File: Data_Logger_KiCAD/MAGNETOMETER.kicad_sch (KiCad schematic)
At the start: 0 parts

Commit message: Sub-schematics Generated
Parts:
- added C17: 10u, symbol Device:C
- added C18: 1u, symbol Device:C
- added U7: MMC5983MA, MMC5983MA_MEM, symbol MMC5983MA_FTP:MMC5983MA
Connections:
- new net: C17.1, U7.10 (CAP)
- new net +3.3V: C18.1, U7.13 (VDDIO), U7.2 (VDD)
- new net GND: C17.2, C18.2, U7.11 (GND), U7.9 (GND)
- new net INT: U7.15 (INT)
- new net SCL/SPI_SCK: U7.1 (SCL/SPI_SCK)
- new net SDA/SPI_SDI: U7.16 (SDA/SPI_SDI)
- new net SPI_CS: U7.4 (SPI_CS)
- new net SPI_SDO: U7.5 (SPI_SDO)
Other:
- company: (none) -> OSU ASDT
- title: (none) -> Magnetometer Schematic

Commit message: Radio Layout V1.0
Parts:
- C17, C18: footprint (none) -> Capacitor_SMD:C_0402_1005Metric
- U7: footprint MMC5983MA_MEM -> footprints:MMC5983MA_MEM
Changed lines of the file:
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@@
 			)
 		)
-		(property "Footprint" ""
+		(property "Footprint" "Capacitor_SMD:C_0402_1005Metric"
 			(at 188.9252 86.36 0)
 			(effects
@@
 			)
 		)
-		(property "Footprint" "MMC5983MA_MEM"
+		(property "Footprint" "footprints:MMC5983MA_MEM"
 			(at 100.33 62.23 0)
 			(effects
@@
 			)
 		)
-		(property "Footprint" ""
+		(property "Footprint" "Capacitor_SMD:C_0402_1005Metric"
 			(at 65.7352 77.47 0)
 			(effects

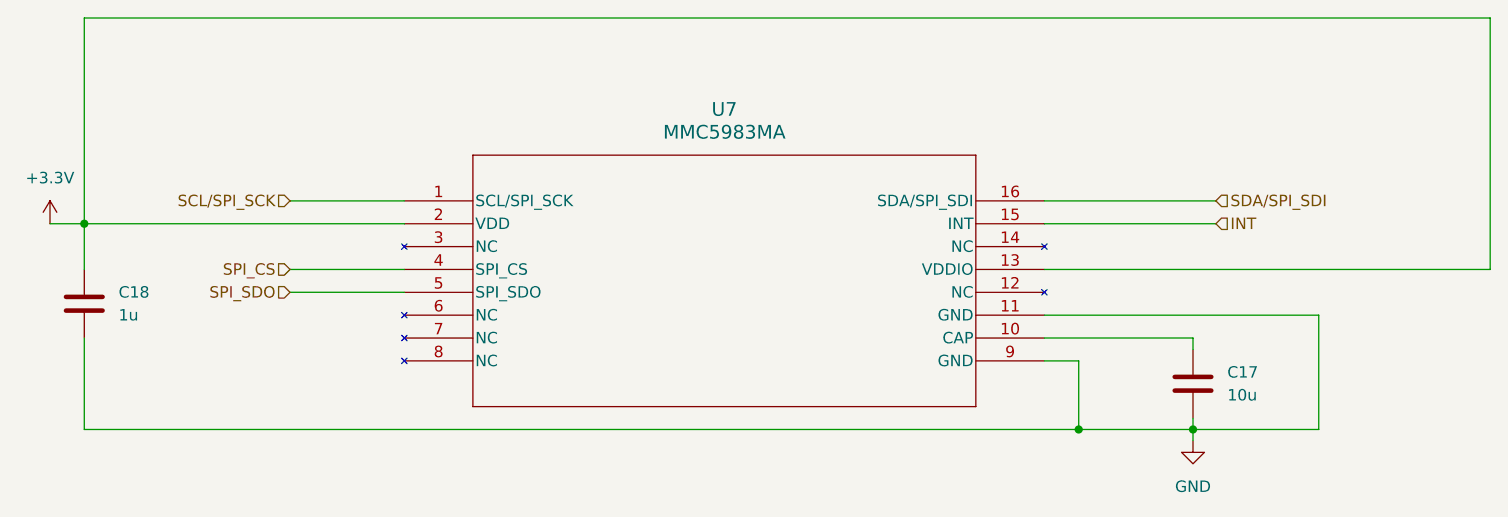
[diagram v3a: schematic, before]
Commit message: Aggregated sub schematics into single primary schematic
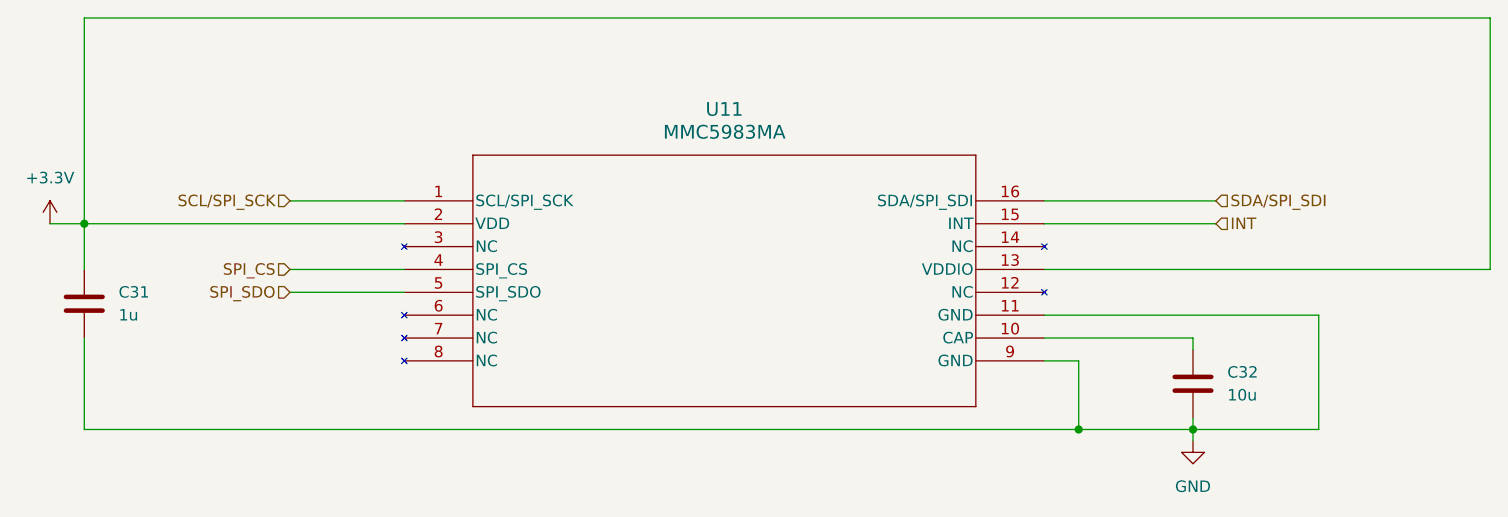
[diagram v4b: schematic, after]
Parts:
- renumbered C18 to C31, C17 to C32, U7 to U11
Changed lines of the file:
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@@
 		(dnp no)
 		(fields_autoplaced yes)
-		(property "Reference" "C17"
+		(property "Reference" "C32"
 			(at 191.77 81.2799 0)
 			(effects
@@
 		)
 		(instances
-			(project ""
-				(path "/db968e42-3ace-4cc9-9096-9d8f48135c40/3c97324b-a98c-481d-b668-72d535313430"
-					(reference "C17")
+			(project "Data_Logger_Board"
+				(path "/db968e42-3ace-4cc9-9096-9d8f48135c40/795ab2be-9db7-4254-b05c-ac2b60177344/884971b6-34e3-480e-b770-6637cf2c2272"
+					(reference "C32")
 					(unit 1)
 				)
@@
 		(dnp no)
 		(fields_autoplaced yes)
-		(property "Reference" "#PWR026"
+		(property "Reference" "#PWR055"
 			(at 60.96 68.58 0)
 			(effects
@@
 		)
 		(instances
-			(project ""
-				(path "/db968e42-3ace-4cc9-9096-9d8f48135c40/3c97324b-a98c-481d-b668-72d535313430"
-					(reference "#PWR026")
+			(project "Data_Logger_Board"
+				(path "/db968e42-3ace-4cc9-9096-9d8f48135c40/795ab2be-9db7-4254-b05c-ac2b60177344/884971b6-34e3-480e-b770-6637cf2c2272"
+					(reference "#PWR055")
 					(unit 1)
 				)
@@
 		(dnp no)
 		(fields_autoplaced yes)
-		(property "Reference" "#PWR025"
+		(property "Reference" "#PWR056"
 			(at 187.96 95.25 0)
 			(effects
@@
 		)
 		(instances
-			(project ""
-				(path "/db968e42-3ace-4cc9-9096-9d8f48135c40/3c97324b-a98c-481d-b668-72d535313430"
-					(reference "#PWR025")
+			(project "Data_Logger_Board"
+				(path "/db968e42-3ace-4cc9-9096-9d8f48135c40/795ab2be-9db7-4254-b05c-ac2b60177344/884971b6-34e3-480e-b770-6637cf2c2272"
+					(reference "#PWR056")
 					(unit 1)
 				)
@@
 		(dnp no)
 		(fields_autoplaced yes)
-		(property "Reference" "U7"
+		(property "Reference" "U11"
 			(at 135.89 52.07 0)
 			(effects
@@
 		)
 		(instances
-			(project ""
-				(path "/db968e42-3ace-4cc9-9096-9d8f48135c40/3c97324b-a98c-481d-b668-72d535313430"
-					(reference "U7")
+			(project "Data_Logger_Board"
+				(path "/db968e42-3ace-4cc9-9096-9d8f48135c40/795ab2be-9db7-4254-b05c-ac2b60177344/884971b6-34e3-480e-b770-6637cf2c2272"
+					(reference "U11")
 					(unit 1)
 				)
@@
 		(dnp no)
 		(fields_autoplaced yes)
-		(property "Reference" "C18"
+		(property "Reference" "C31"
 			(at 68.58 72.3899 0)
 			(effects
@@
 		(instances
 			(project "Data_Logger_Board"
-				(path "/db968e42-3ace-4cc9-9096-9d8f48135c40/3c97324b-a98c-481d-b668-72d535313430"
-					(reference "C18")
-					(unit 1)
-				)
+				(path "/db968e42-3ace-4cc9-9096-9d8f48135c40/795ab2be-9db7-4254-b05c-ac2b60177344/884971b6-34e3-480e-b770-6637cf2c2272"
+					(reference "C31")
+					(unit 1)
+				)

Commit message: update changes to MCU, add gitignore
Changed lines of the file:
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@@
 	)
 	(hierarchical_label "SPI_SDO"
-		(shape input)
+		(shape output)
 		(at 87.63 72.39 180)
 		(effects

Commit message: rem old files and add LCSC #'s
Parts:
- C31: LCSC (none) -> C52923
- C32: LCSC (none) -> C15525
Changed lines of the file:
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@@
+			)
+		)
+		(property "LCSC" "C15525"
+			(at 187.96 82.55 0)
+			(effects
+				(font
+					(size 1.27 1.27)
+				)
+				(hide yes)
 			)
 		)
@@
 			(at 64.77 73.66 0)
 			(effects
+				(font
+					(size 1.27 1.27)
+				)
+				(hide yes)
+			)
+		)
+		(property "LCSC" "C52923"
+			(at 64.77 73.66 0)
+			(effects

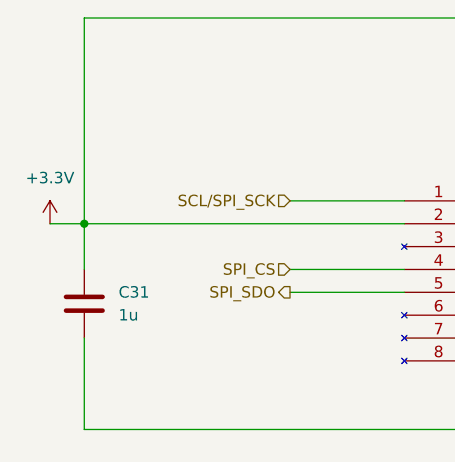
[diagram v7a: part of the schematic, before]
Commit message: more progress on MCU layout
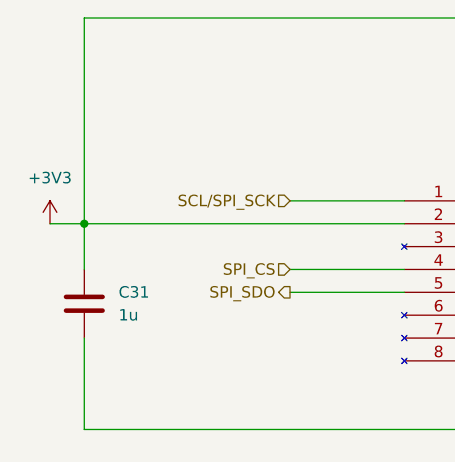
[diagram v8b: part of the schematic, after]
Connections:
- net +3.3V renamed +3V3
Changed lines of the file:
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@@
 			)
 		)
-		(property "Value" "+3.3V"
+		(property "Value" "+3V3"
 			(at 60.96 59.69 0)
 			(effects
